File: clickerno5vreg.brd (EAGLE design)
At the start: 89 x 20 mm, 50 parts, among them IC1 DW01A, IC2 TP4056, J1 DX07S016JA1R1500, Q1 FS8205A, U1 TPS61040DBVR, Y1 16MHz

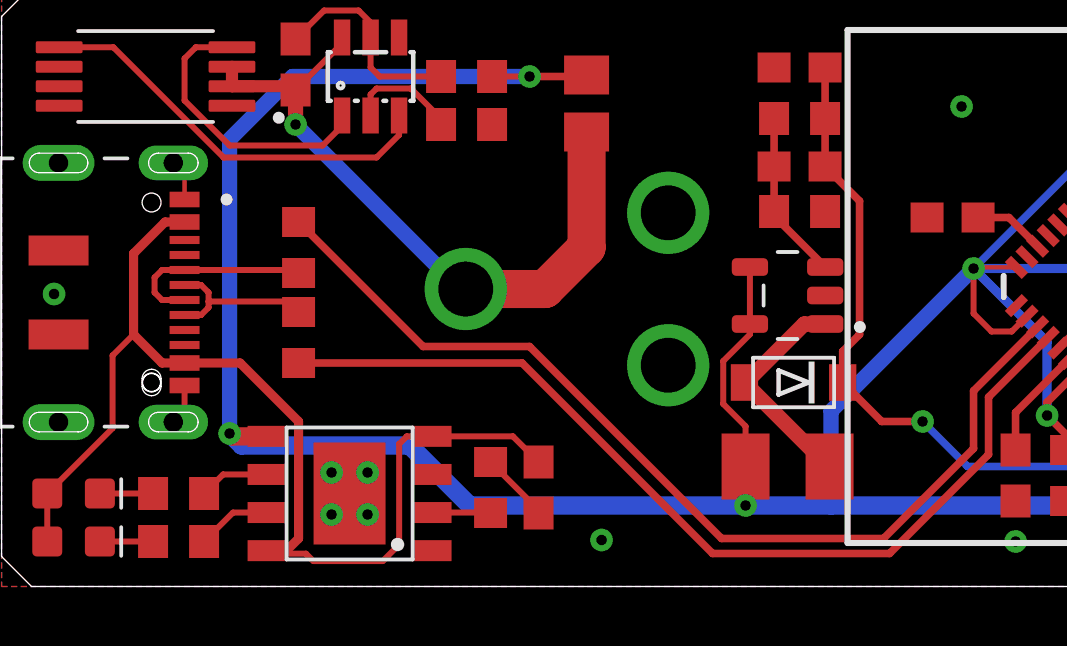
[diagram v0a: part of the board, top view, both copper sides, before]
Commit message: added pd resistors
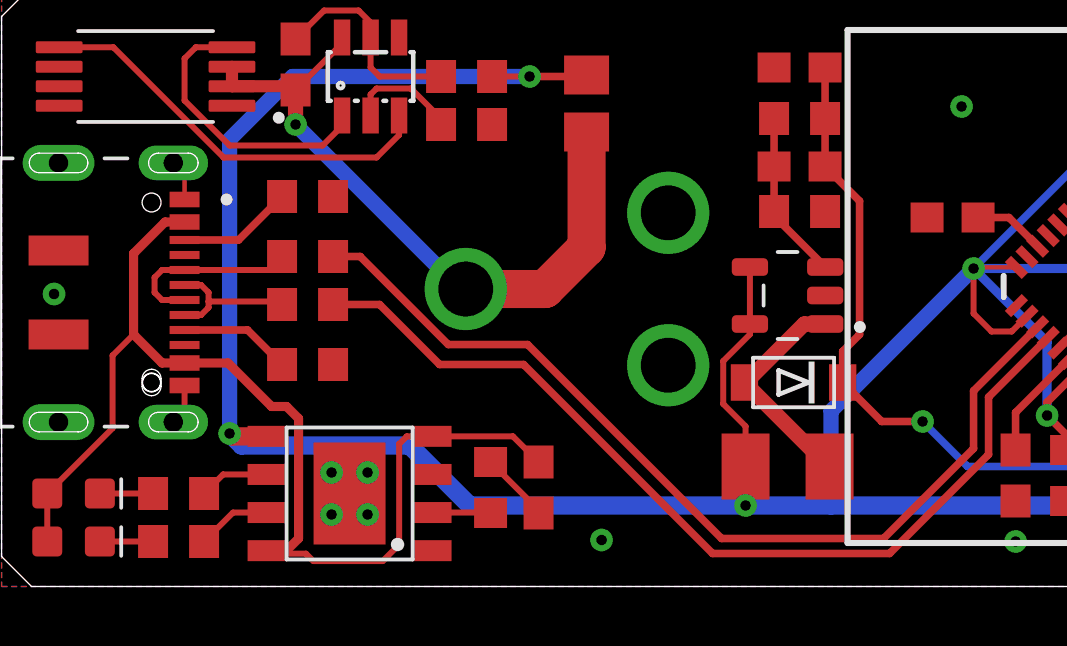
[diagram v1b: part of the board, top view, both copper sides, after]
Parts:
- added R17, R18: (no value), rcl:R0603
- moved R1 1.14 mm to (10.2, 9.40), turned to 0 degrees
- moved R2 0.42 mm to (10.2, 11.0), turned to 0 degrees
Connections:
- new net N$31: J1.3, R17.1
- new net N$32: J1.9, R18.1
- net GND: now also R17.2, R18.2
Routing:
- net N$31: track 0.00 -> 3.85 mm
- net N$32: track 0.00 -> 3.73 mm
- net N$6: track 33.1 -> 31.4 mm
- net N$3: track 5.45 -> 4.80 mm
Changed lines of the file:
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@@
 <setting verticaltext="up"/>
 </settings>
-<grid distance="1" unitdist="mm" unit="mm" style="lines" multiple="1" display="yes" altdistance="5" altunitdist="mil" altunit="mil"/>
+<grid distance="0.1" unitdist="mm" unit="mm" style="lines" multiple="1" display="yes" altdistance="5" altunitdist="mil" altunit="mil"/>
 <layers>
 <layer number="1" name="Top" color="4" fill="1" visible="yes" active="yes"/>
@@
 <attribute name="PURCHASE-URL" value="https://pricing.snapeda.com/search/part/DX07S016JA1R1500/?ref=eda" x="5" y="9.8" size="1.778" layer="27" rot="R270" display="off"/>
 </element>
-<element name="R1" library="rcl" library_urn="urn:adsk.eagle:library:334" package="R0603" package3d_urn="urn:adsk.eagle:package:23555/3" value="22" x="9.9" y="8.3" smashed="yes" rot="R270">
-<attribute name="POPULARITY" value="70" x="9.9" y="8.3" size="1.778" layer="27" rot="R270" display="off"/>
-<attribute name="SPICEPREFIX" value="R" x="9.9" y="8.3" size="1.778" layer="27" rot="R270" display="off"/>
-</element>
-<element name="R2" library="rcl" library_urn="urn:adsk.eagle:library:334" package="R0603" package3d_urn="urn:adsk.eagle:package:23555/3" value="22" x="9.9" y="11.3" smashed="yes" rot="R90">
-<attribute name="POPULARITY" value="70" x="9.9" y="11.3" size="1.778" layer="27" rot="R90" display="off"/>
-<attribute name="SPICEPREFIX" value="R" x="9.9" y="11.3" size="1.778" layer="27" rot="R90" display="off"/>
+<element name="R1" library="rcl" library_urn="urn:adsk.eagle:library:334" package="R0603" package3d_urn="urn:adsk.eagle:package:23555/3" value="22" x="10.2" y="9.4" smashed="yes">
+<attribute name="POPULARITY" value="70" x="10.2" y="9.4" size="1.778" layer="27" display="off"/>
+<attribute name="SPICEPREFIX" value="R" x="10.2" y="9.4" size="1.778" layer="27" display="off"/>
+</element>
+<element name="R2" library="rcl" library_urn="urn:adsk.eagle:library:334" package="R0603" package3d_urn="urn:adsk.eagle:package:23555/3" value="22" x="10.2" y="11" smashed="yes">
+<attribute name="POPULARITY" value="70" x="10.2" y="11" size="1.778" layer="27" display="off"/>
+<attribute name="SPICEPREFIX" value="R" x="10.2" y="11" size="1.778" layer="27" display="off"/>
 </element>
 <element name="Y1" library="SparkFun-Clocks" library_urn="urn:adsk.eagle:library:511" package="CRYSTAL-SMD-5X3.2-4PAD" package3d_urn="urn:adsk.eagle:package:37518/1" value="16MHz" x="48.7" y="10" smashed="yes" rot="R90">
@@
 <attribute name="POPULARITY" value="21" x="84.5" y="4.5" size="1.778" layer="28" rot="MR90" display="off"/>
 <attribute name="VALUE" x="84.5" y="4.5" size="0.0254" layer="28" rot="MR90"/>
+</element>
+<element name="R17" library="rcl" library_urn="urn:adsk.eagle:library:334" package="R0603" package3d_urn="urn:adsk.eagle:package:23555/3" value="" x="10.2" y="13" smashed="yes">
+<attribute name="POPULARITY" value="70" x="10.2" y="13" size="1.778" layer="27" display="off"/>
+<attribute name="SPICEPREFIX" value="R" x="10.2" y="13" size="1.778" layer="27" display="off"/>
+<attribute name="VALUE" x="9.565" y="11.095" size="1.27" layer="27"/>
+</element>
+<element name="R18" library="rcl" library_urn="urn:adsk.eagle:library:334" package="R0603" package3d_urn="urn:adsk.eagle:package:23555/3" value="" x="10.2" y="7.4" smashed="yes">
+<attribute name="POPULARITY" value="70" x="10.2" y="7.4" size="1.778" layer="27" display="off"/>
+<attribute name="SPICEPREFIX" value="R" x="10.2" y="7.4" size="1.778" layer="27" display="off"/>
+<attribute name="VALUE" x="9.565" y="5.495" size="1.27" layer="27"/>
 </element>
 </elements>
@@
 <wire x1="6.1" y1="13.745" x2="5.725" y2="14.12" width="0.1524" layer="1"/>
 <via x="12.2" y="2.4" extent="1-16" drill="0.35"/>
+<contactref element="R18" pad="2"/>
+<contactref element="R17" pad="2"/>
 </signal>
 <signal name="N$1">
@@
 <contactref element="J1" pad="8"/>
 <contactref element="R1" pad="1"/>
-<wire x1="9.875" y1="9.175" x2="9.9" y2="9.15" width="0.2" layer="1"/>
 <wire x1="6.1" y1="10.05" x2="6.65" y2="10.05" width="0.2" layer="1"/>
 <wire x1="6.65" y1="10.05" x2="6.9" y2="9.8" width="0.2" layer="1"/>
@@
 <wire x1="6.9" y1="9.8" x2="6.9" y2="9.5" width="0.2" layer="1"/>
 <wire x1="6.9" y1="9.5" x2="6.9" y2="9.3" width="0.2" layer="1"/>
-<wire x1="6.9" y1="9.5" x2="9.55" y2="9.5" width="0.2" layer="1"/>
-<wire x1="9.55" y1="9.5" x2="9.875" y2="9.175" width="0.2" layer="1"/>
+<wire x1="6.9" y1="9.5" x2="9.25" y2="9.5" width="0.2" layer="1"/>
+<wire x1="9.25" y1="9.5" x2="9.35" y2="9.4" width="0.2" layer="1"/>
 </signal>
 <signal name="N$4">
@@
 <contactref element="J1" pad="5"/>
 <contactref element="R2" pad="1"/>
-<wire x1="6.1" y1="10.55" x2="9.8" y2="10.55" width="0.2" layer="1"/>
-<wire x1="9.8" y1="10.55" x2="9.9" y2="10.45" width="0.2" layer="1"/>
 <wire x1="5.35" y1="10.55" x2="5.1" y2="10.3" width="0.2" layer="1"/>
 <wire x1="5.35" y1="10.55" x2="6.1" y2="10.55" width="0.2" layer="1"/>
@@
 <wire x1="5.1" y1="9.8" x2="5.35" y2="9.55" width="0.2" layer="1"/>
 <wire x1="5.35" y1="9.55" x2="6.1" y2="9.55" width="0.2" layer="1"/>
+<wire x1="6.1" y1="10.55" x2="8.9" y2="10.55" width="0.2" layer="1"/>
+<wire x1="8.9" y1="10.55" x2="9.35" y2="11" width="0.2" layer="1"/>
 </signal>
 <signal name="N$5">
@@
 <wire x1="29.6" y1="1.1" x2="32.9" y2="4.4" width="0.254" layer="1"/>
 <wire x1="32.9" y1="6.3142125" x2="34.888728125" y2="8.302940625" width="0.254" layer="1"/>
-<wire x1="9.9" y1="7.45" x2="17.35" y2="7.45" width="0.254" layer="1"/>
-<wire x1="17.35" y1="7.45" x2="23.7" y2="1.1" width="0.254" layer="1"/>
+<wire x1="23.7" y1="1.1" x2="17.4" y2="7.4" width="0.254" layer="1"/>
 <wire x1="32.9" y1="4.4" x2="32.9" y2="6.3142125" width="0.254" layer="1"/>
+<wire x1="17.4" y1="7.4" x2="14.6" y2="7.4" width="0.254" layer="1"/>
+<wire x1="14.6" y1="7.4" x2="12.6" y2="9.4" width="0.254" layer="1"/>
+<wire x1="12.6" y1="9.4" x2="11.05" y2="9.4" width="0.254" layer="1"/>
 </signal>
 <signal name="N$6">
 <contactref element="R2" pad="2"/>
 <contactref element="U$1" pad="3"/>
-<wire x1="9.9" y1="12.15" x2="14.05" y2="8" width="0.254" layer="1"/>
-<wire x1="24" y1="1.6" x2="29.4" y2="1.6" width="0.254" layer="1"/>
+<wire x1="29.4" y1="1.6" x2="24" y2="1.6" width="0.254" layer="1"/>
 <wire x1="29.4" y1="1.6" x2="32.4" y2="4.6" width="0.254" layer="1"/>
-<wire x1="14.05" y1="8" x2="17.6" y2="8" width="0.254" layer="1"/>
-<wire x1="17.6" y1="8" x2="24" y2="1.6" width="0.254" layer="1"/>
 <wire x1="32.4" y1="6.521321875" x2="34.535175" y2="8.656496875" width="0.254" layer="1"/>
 <wire x1="32.4" y1="4.6" x2="32.4" y2="6.521321875" width="0.254" layer="1"/>
+<wire x1="11.95413125" y1="11" x2="11.05" y2="11" width="0.254" layer="1"/>
+<wire x1="17.535" y1="8.065" x2="14.88913125" y2="8.065" width="0.254" layer="1"/>
+<wire x1="14.88913125" y1="8.065" x2="11.95413125" y2="11" width="0.254" layer="1"/>
+<wire x1="24" y1="1.6" x2="17.535" y2="8.065" width="0.254" layer="1"/>
 </signal>
 <signal name="N$7">
@@
 <wire x1="5.35" y1="7.45" x2="6.1" y2="7.45" width="0.3048" layer="1"/>
 <wire x1="5.45" y1="12.15" x2="6.1" y2="12.15" width="0.3048" layer="1"/>
-<wire x1="6.1" y1="7.45" x2="7.95" y2="7.45" width="0.3048" layer="1"/>
-<wire x1="7.95" y1="7.45" x2="9.9" y2="5.5" width="0.3048" layer="1"/>
-<wire x1="9.9" y1="5.5" x2="9.9" y2="1.6" width="0.3048" layer="1"/>
 <wire x1="9.495" y1="1.195" x2="8.85" y2="1.195" width="0.3048" layer="1"/>
 <wire x1="9.9" y1="1.6" x2="9.495" y2="1.195" width="0.3048" layer="1"/>
@@
 <wire x1="13.505" y1="5.005" x2="14.35" y2="5.005" width="0.2" layer="1"/>
 <wire x1="13.25265" y1="4.75265" x2="13.505" y2="5.005" width="0.2" layer="1"/>
+<wire x1="7.55" y1="7.45" x2="9" y2="6" width="0.3048" layer="1"/>
+<wire x1="9" y1="6" x2="9.5" y2="6" width="0.3048" layer="1"/>
+<wire x1="9.5" y1="6" x2="9.9" y2="5.6" width="0.3048" layer="1"/>
+<wire x1="6.1" y1="7.45" x2="7.55" y2="7.45" width="0.3048" layer="1"/>
+<wire x1="9.9" y1="5.6" x2="9.9" y2="1.6" width="0.3048" layer="1"/>
+</signal>
+<signal name="N$31">
+<contactref element="J1" pad="3"/>
+<contactref element="R17" pad="1"/>
+<wire x1="6.1" y1="11.55" x2="7.9" y2="11.55" width="0.254" layer="1"/>
+<wire x1="7.9" y1="11.55" x2="9.35" y2="13" width="0.254" layer="1"/>
+</signal>
+<signal name="N$32">
+<contactref element="J1" pad="9"/>
+<contactref element="R18" pad="1"/>
+<wire x1="6.1" y1="8.55" x2="8.2" y2="8.55" width="0.254" layer="1"/>
+<wire x1="8.2" y1="8.55" x2="9.35" y2="7.4" width="0.254" layer="1"/>
 </signal>
 </signals>
